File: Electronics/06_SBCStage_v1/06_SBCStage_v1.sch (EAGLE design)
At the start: 33 parts, among them J3 CONN_2X3_SMD, J4 BARRIER_BLOCK-3PIN, U1 XL4016-DEV

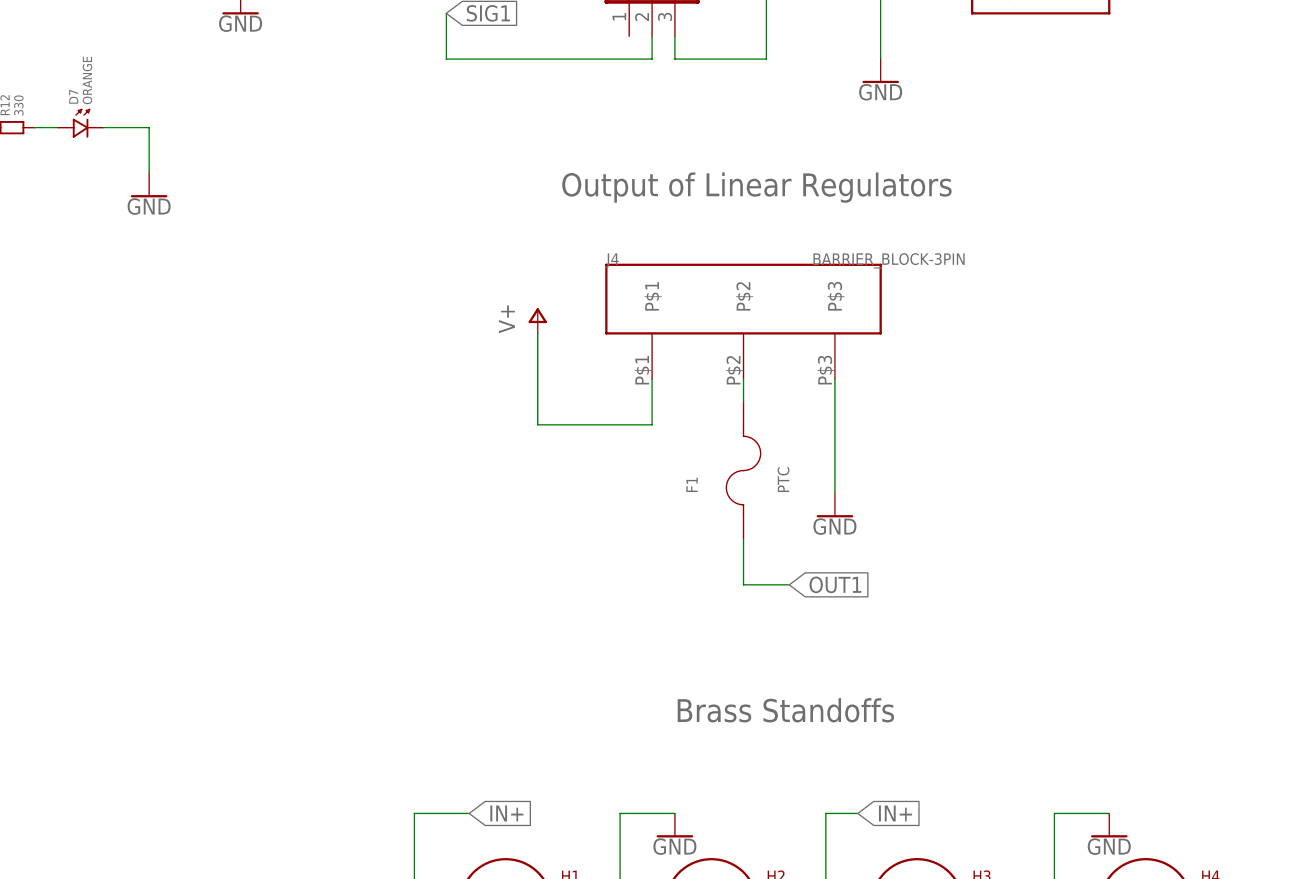
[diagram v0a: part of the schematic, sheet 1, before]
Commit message: SBC stage: Moved test point to after the PTC fuse
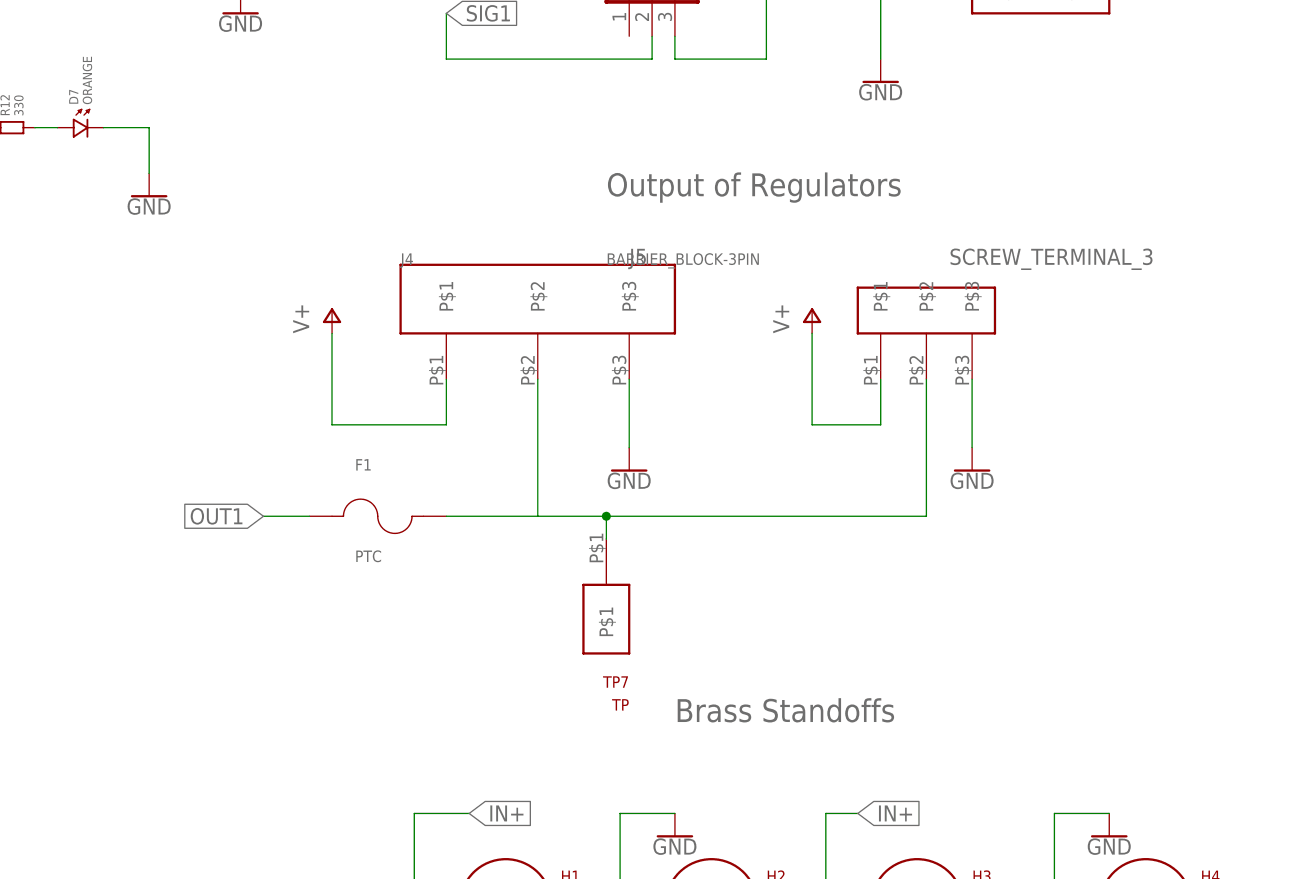
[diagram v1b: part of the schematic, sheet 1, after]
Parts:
- added J5: SCREW_TERMINAL_3, EK's Parts:SCREW_TERMINAL_3
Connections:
- net GND: now also J5.P$3
- net N$2: now also J5.P$2, TP7.P$1
- net OUT1: no longer TP7.P$1
- net V+: now also J5.P$1
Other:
- note added: "Output of Regulators"
- note removed: "Output of Linear Regulators"
- moved on the sheet: F1, J4
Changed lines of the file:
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@@
 <part name="C3" library="standardparts" deviceset="CAPACITOR" device=".1206" value="10 uF"/>
 <part name="C4" library="standardparts" deviceset="CAPACITOR" device=".1206" value="22 uF"/>
-<part name="TP7" library="Hippo-PS" deviceset="TP" device=""/>
 <part name="R6" library="standardparts" deviceset="RESISTOR" device=".1206" value="10K"/>
 <part name="R7" library="standardparts" deviceset="RESISTOR" device=".1206" value="10K"/>
@@
 <part name="J2" library="SparkFun-Connectors" library_urn="urn:adsk.eagle:library:513" deviceset="CONN_03" device="" package3d_urn="urn:adsk.eagle:package:38063/1"/>
 <part name="F1" library="Hippo-PS" deviceset="PTC" device=""/>
+<part name="J5" library="EK's Parts" deviceset="SCREW_TERMINAL_3" device=""/>
+<part name="GND8" library="SparkFun-PowerSymbols" library_urn="urn:adsk.eagle:library:530" deviceset="GND" device=""/>
+<part name="P+2" library="supply1" library_urn="urn:adsk.eagle:library:371" deviceset="V+" device=""/>
+<part name="TP7" library="Hippo-PS" deviceset="TP" device=""/>
 </parts>
 <sheets>
@@
 (for switching regulator)</text>
 <text x="149.86" y="175.26" size="2.54" layer="95">Header Interface to Power Management Board</text>
-<text x="162.56" y="124.46" size="2.54" layer="95">Output of Linear Regulators</text>
+<text x="167.64" y="124.46" size="2.54" layer="95">Output of Regulators</text>
 <text x="175.26" y="66.04" size="2.54" layer="95">Brass Standoffs</text>
 <text x="10.16" y="66.04" size="2.54" layer="95">Testpoints (Switching V+, Battery In+)</text>
@@
 <attribute name="VALUE" x="116.84" y="124.206" size="1.778" layer="96" align="top-center"/>
 </instance>
-<instance part="J4" gate="G$1" x="182.88" y="114.3" smashed="yes">
-<attribute name="NAME" x="167.64" y="116.84" size="1.27" layer="95"/>
-<attribute name="VALUE" x="190.5" y="116.84" size="1.27" layer="96"/>
-</instance>
-<instance part="P+3" gate="1" x="160.02" y="111.76" smashed="yes">
-<attribute name="VALUE" x="157.48" y="109.22" size="1.778" layer="96" rot="R90"/>
-</instance>
-<instance part="GND1" gate="1" x="193.04" y="88.9" smashed="yes">
-<attribute name="VALUE" x="193.04" y="88.646" size="1.778" layer="96" align="top-center"/>
+<instance part="J4" gate="G$1" x="160.02" y="114.3" smashed="yes">
+<attribute name="NAME" x="144.78" y="116.84" size="1.27" layer="95"/>
+<attribute name="VALUE" x="167.64" y="116.84" size="1.27" layer="96"/>
+</instance>
+<instance part="P+3" gate="1" x="137.16" y="111.76" smashed="yes">
+<attribute name="VALUE" x="134.62" y="109.22" size="1.778" layer="96" rot="R90"/>
+</instance>
+<instance part="GND1" gate="1" x="170.18" y="93.98" smashed="yes">
+<attribute name="VALUE" x="170.18" y="93.726" size="1.778" layer="96" align="top-center"/>
 </instance>
 <instance part="J1" gate="J$1" x="172.72" y="167.64" smashed="yes" rot="R270">
@@
 <attribute name="NAME" x="178.308" y="152.4" size="1.778" layer="95" font="vector" rot="R270"/>
 </instance>
-<instance part="F1" gate="G$1" x="182.88" y="93.98" smashed="yes" rot="R90">
-<attribute name="NAME" x="177.8" y="91.44" size="1.27" layer="95" rot="R90"/>
-<attribute name="VALUE" x="187.96" y="91.44" size="1.27" layer="96" rot="R90"/>
+<instance part="F1" gate="G$1" x="142.24" y="88.9" smashed="yes">
+<attribute name="NAME" x="139.7" y="93.98" size="1.27" layer="95"/>
+<attribute name="VALUE" x="139.7" y="83.82" size="1.27" layer="96"/>
+</instance>
+<instance part="J5" gate="G$1" x="203.2" y="111.76" smashed="yes">
+<attribute name="NAME" x="170.18" y="116.84" size="1.778" layer="95"/>
+<attribute name="VALUE" x="205.74" y="116.84" size="1.778" layer="96"/>
+</instance>
+<instance part="GND8" gate="1" x="208.28" y="93.98" smashed="yes">
+<attribute name="VALUE" x="208.28" y="93.726" size="1.778" layer="96" align="top-center"/>
+</instance>
+<instance part="P+2" gate="1" x="190.5" y="111.76" smashed="yes">
+<attribute name="VALUE" x="187.96" y="109.22" size="1.778" layer="96" rot="R90"/>
+</instance>
+<instance part="TP7" gate="G$1" x="167.64" y="81.28" smashed="yes" rot="R180">
+<attribute name="NAME" x="170.18" y="71.12" size="1.27" layer="94" rot="R180"/>
+<attribute name="VALUE" x="170.18" y="68.58" size="1.27" layer="94" rot="R180"/>
 </instance>
 </instances>
@@
 <segment>
 <pinref part="P+3" gate="1" pin="V+"/>
-<wire x1="160.02" y1="109.22" x2="160.02" y2="99.06" width="0.1524" layer="91"/>
-<wire x1="160.02" y1="99.06" x2="172.72" y2="99.06" width="0.1524" layer="91"/>
+<wire x1="137.16" y1="109.22" x2="137.16" y2="99.06" width="0.1524" layer="91"/>
+<wire x1="137.16" y1="99.06" x2="149.86" y2="99.06" width="0.1524" layer="91"/>
 <pinref part="J4" gate="G$1" pin="P$1"/>
-<wire x1="172.72" y1="99.06" x2="172.72" y2="104.14" width="0.1524" layer="91"/>
+<wire x1="149.86" y1="99.06" x2="149.86" y2="104.14" width="0.1524" layer="91"/>
+</segment>
+<segment>
+<pinref part="P+2" gate="1" pin="V+"/>
+<wire x1="190.5" y1="109.22" x2="190.5" y2="99.06" width="0.1524" layer="91"/>
+<wire x1="190.5" y1="99.06" x2="198.12" y2="99.06" width="0.1524" layer="91"/>
+<pinref part="J5" gate="G$1" pin="P$1"/>
+<wire x1="198.12" y1="104.14" x2="198.12" y2="99.06" width="0.1524" layer="91"/>
 </segment>
 </net>
@@
 <segment>
 <pinref part="J4" gate="G$1" pin="P$3"/>
-<wire x1="193.04" y1="104.14" x2="193.04" y2="91.44" width="0.1524" layer="91"/>
+<wire x1="170.18" y1="104.14" x2="170.18" y2="96.52" width="0.1524" layer="91"/>
 <pinref part="GND1" gate="1" pin="GND"/>
+</segment>
+<segment>
+<pinref part="J5" gate="G$1" pin="P$3"/>
+<wire x1="208.28" y1="104.14" x2="208.28" y2="96.52" width="0.1524" layer="91"/>
+<pinref part="GND8" gate="1" pin="GND"/>
 </segment>
 </net>
@@
 <net name="OUT1" class="0">
 <segment>
-<label x="187.96" y="81.28" size="1.778" layer="95" xref="yes"/>
+<label x="129.54" y="88.9" size="1.778" layer="95" rot="R180" xref="yes"/>
 <pinref part="F1" gate="G$1" pin="1"/>
-<wire x1="182.88" y1="86.36" x2="182.88" y2="81.28" width="0.1524" layer="91"/>
-<wire x1="182.88" y1="81.28" x2="187.96" y2="81.28" width="0.1524" layer="91"/>
+<wire x1="134.62" y1="88.9" x2="129.54" y2="88.9" width="0.1524" layer="91"/>
 </segment>
 </net>
@@
 <segment>
 <pinref part="J4" gate="G$1" pin="P$2"/>
+<wire x1="160.02" y1="104.14" x2="160.02" y2="88.9" width="0.1524" layer="91"/>
+<pinref part="J5" gate="G$1" pin="P$2"/>
+<wire x1="160.02" y1="88.9" x2="167.64" y2="88.9" width="0.1524" layer="91"/>
+<wire x1="167.64" y1="88.9" x2="203.2" y2="88.9" width="0.1524" layer="91"/>
+<wire x1="203.2" y1="88.9" x2="203.2" y2="104.14" width="0.1524" layer="91"/>
 <pinref part="F1" gate="G$1" pin="2"/>
-<wire x1="182.88" y1="104.14" x2="182.88" y2="101.6" width="0.1524" layer="91"/>
+<wire x1="160.02" y1="88.9" x2="149.86" y2="88.9" width="0.1524" layer="91"/>
+<pinref part="TP7" gate="G$1" pin="P$1"/>
+<wire x1="167.64" y1="86.36" x2="167.64" y2="88.9" width="0.1524" layer="91"/>
+<junction x="167.64" y="88.9"/>
 </segment>
 </net>
@@
 <attribute name="VALUE" x="74.295" y="140.97" size="1.016" layer="96" rot="R180"/>
 </instance>
-<instance part="TP7" gate="G$1" x="93.98" y="142.24" smashed="yes" rot="R180">
-<attribute name="NAME" x="96.52" y="132.08" size="1.27" layer="94" rot="R180"/>
-<attribute name="VALUE" x="96.52" y="129.54" size="1.27" layer="94" rot="R180"/>
-</instance>
 <instance part="R6" gate="G$1" x="116.84" y="144.78" smashed="yes" rot="R90">
 <attribute name="NAME" x="115.57" y="143.51" size="1.016" layer="95" rot="MR0"/>
@@
 <pinref part="R13" gate="G$1" pin="1"/>
 <wire x1="104.14" y1="142.24" x2="104.14" y2="152.4" width="0.1524" layer="91"/>
-<wire x1="83.82" y1="152.4" x2="93.98" y2="152.4" width="0.1524" layer="91"/>
 <junction x="83.82" y="152.4"/>
-<pinref part="TP7" gate="G$1" pin="P$1"/>
-<wire x1="93.98" y1="152.4" x2="104.14" y2="152.4" width="0.1524" layer="91"/>
-<wire x1="93.98" y1="147.32" x2="93.98" y2="152.4" width="0.1524" layer="91"/>
-<junction x="93.98" y="152.4"/>
+<wire x1="83.82" y1="152.4" x2="104.14" y2="152.4" width="0.1524" layer="91"/>
 <wire x1="104.14" y1="152.4" x2="116.84" y2="152.4" width="0.1524" layer="91"/>
 <junction x="104.14" y="152.4"/>

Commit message: Naming update to Hippo-PD
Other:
- note added: "Hippo-PD Motor Stage Designed by: Erin Kennedy July 9, 2022"
- note added: "Hippo-PD SBC Stage Designed by: Erin Kennedy July 13, 2022"
- note removed: "Hippo-PS Motor Stage Designed by: Erin Kennedy July 9, 2022"
- note removed: "Hippo-PS SBC Stage Designed by: Erin Kennedy July 13, 2022"
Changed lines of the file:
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@@
 <text x="175.26" y="66.04" size="2.54" layer="95">Brass Standoffs</text>
 <text x="10.16" y="66.04" size="2.54" layer="95">Testpoints (Switching V+, Battery In+)</text>
-<text x="149.86" y="25.4" size="1.778" layer="95">Hippo-PS SBC Stage
+<text x="149.86" y="25.4" size="1.778" layer="95">Hippo-PD SBC Stage
 Designed by: Erin Kennedy
 July 13, 2022</text>
@@
 <plain>
 <text x="55.88" y="170.18" size="2.54" layer="95">Linear Regulator (5V)</text>
-<text x="149.86" y="25.4" size="1.778" layer="95">Hippo-PS Motor Stage
+<text x="149.86" y="25.4" size="1.778" layer="95">Hippo-PD Motor Stage
 Designed by: Erin Kennedy
 July 9, 2022</text>

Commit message: SBC stage electronics v1 final
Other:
- note removed: "Hippo-PD Motor Stage Designed by: Erin Kennedy July 9, 2022"
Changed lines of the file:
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@@
 <plain>
 <text x="55.88" y="170.18" size="2.54" layer="95">Linear Regulator (5V)</text>
-<text x="149.86" y="25.4" size="1.778" layer="95">Hippo-PD Motor Stage
+<text x="149.86" y="25.4" size="1.778" layer="95">Hippo-PD SBC Stage
 Designed by: Erin Kennedy
-July 9, 2022</text>
+July 13, 2022</text>
 </plain>
 <instances>
